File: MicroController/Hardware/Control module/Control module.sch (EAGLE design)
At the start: 78 parts, among them J1 1X2-3.5MM, J2 RJ45-TRAFO, J3 RJ45-TRAFO, J4 RJ45-TRAFO, J6 RJ11, Q1 BSS138, Q2 BSS138, Q3 BSS138, Q4 BSS138, Q5 BSS138, Q6 BSS138, Q7 BSS138, Q8 BSS138, U1 CD74HC4067SM96, U3 TLV1117-33CDCY

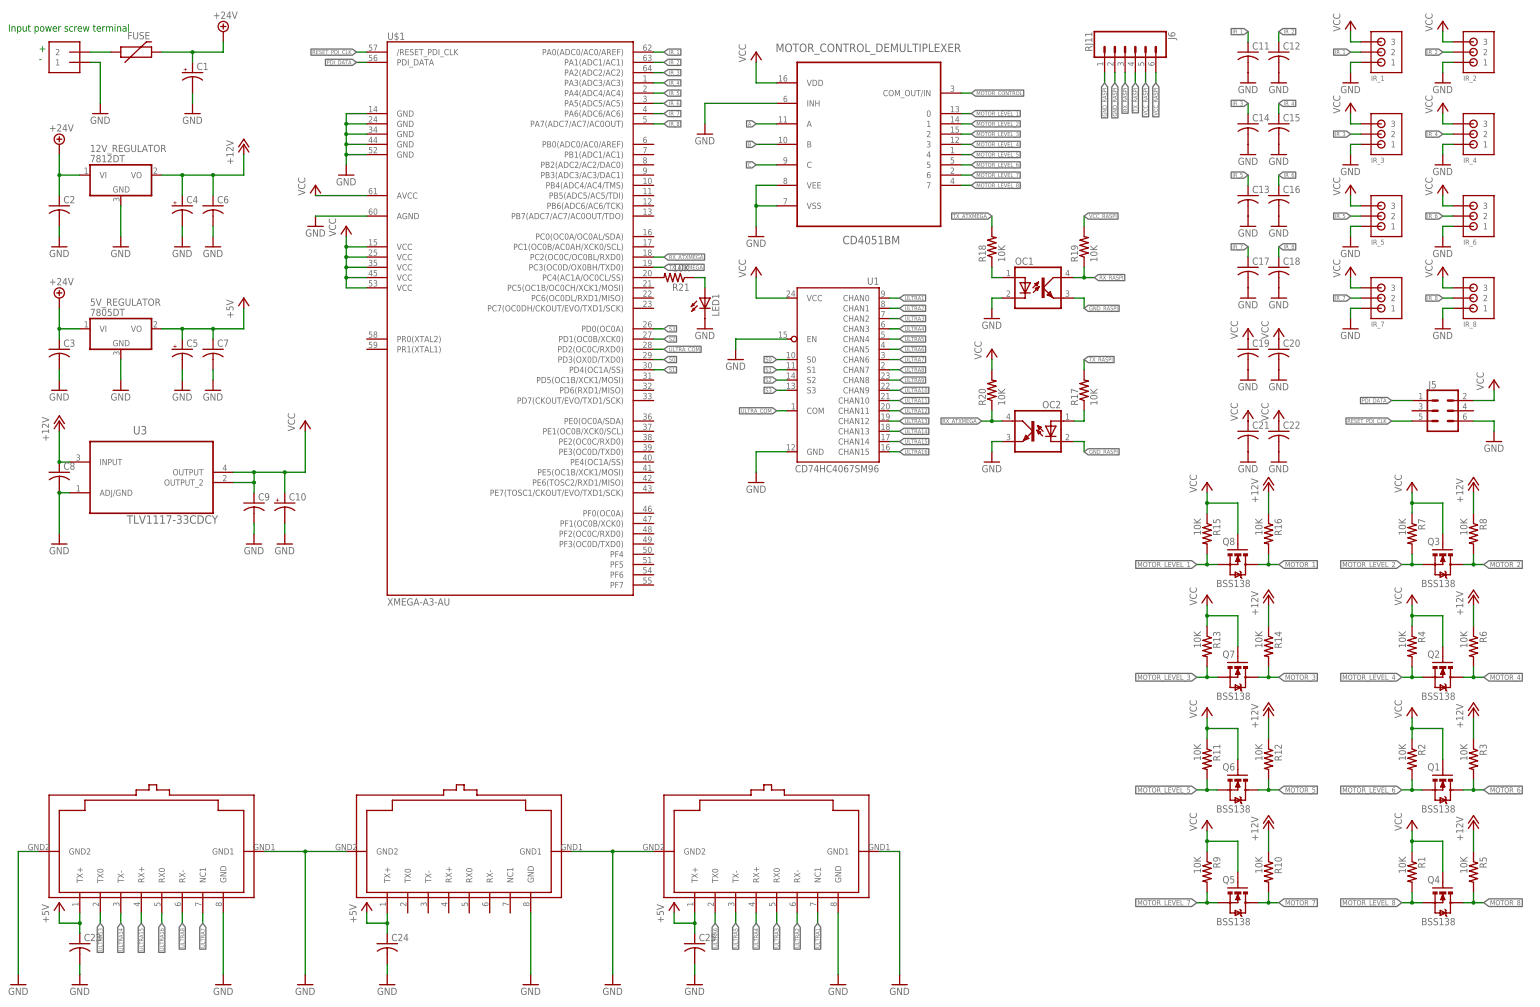
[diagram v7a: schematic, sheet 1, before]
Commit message: Changed many things in the layout.
Added more I/O and connectivity to the Raspberry Pi.
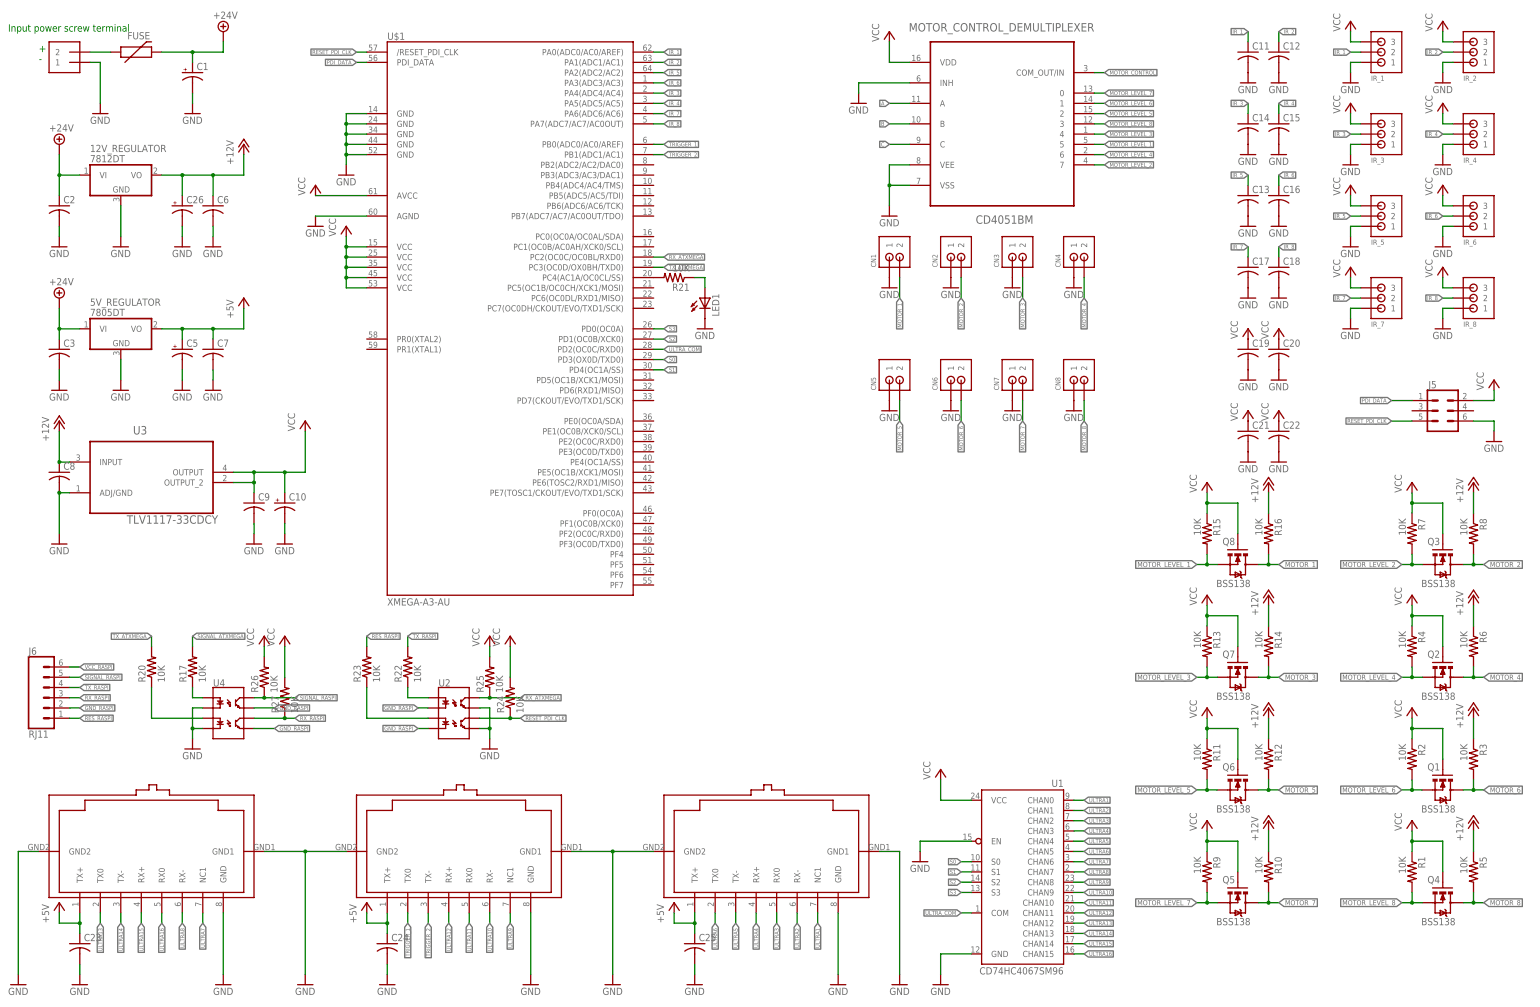
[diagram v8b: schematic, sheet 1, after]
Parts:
- removed C4: (no value), adafruit:CPOL-USE2.5-6
- removed OC1, OC2: (no value), optocoupler:PC817
- removed R18, R19: 10K, adafruit:R-US_R0805
- added C26: (no value), adafruit:CPOL-US175TMP-0810
- added CN1, CN2, CN3, CN4, CN5, CN6, CN7, CN8: JST-PH_2-PIN_HEADER, SRG:JST-PH_2-PIN_HEADER
- added R22, R23, R24, R25, R26, R27: 10K, adafruit:R-US_R0805
- added U2, U4: DUAL-OPTOISOLATOR_SOIC8, SparkFun-DiscreteSemi:DUAL-OPTOISOLATOR_SOIC8
- C1: device adafruit:CPOL-USE5-10.5 -> adafruit:CPOL-US175TMP-0810
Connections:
- removed net N$1: OC1.A, R18.1
- new net N$5: R23.1, U2.A2
- new net N$6: R22.1, U2.A1
- new net N$8: R20.1, U4.A2
- new net RES_RASPI: J6.1, R23.2
- new net SIGNAL_ATXMEGA: R17.2
- new net SIGNAL_RASPI: J6.5, R26.1, U4.CL1
- new net TRIGGER_1: J4.TX0, U$1.PB0(ADC0/AC0/AREF)
- new net TRIGGER_2: J4.TX-, U$1.PB1(ADC1/AC1)
- net +12V: now also C26.+; no longer C4.+
- net GND: now also C26.-, CN1.1, CN2.1, CN3.1, CN4.1, CN5.1, CN6.1, CN7.1, CN8.1, U2.EM1, U2.EM2, U4.C1, U4.C2; no longer C4.-, OC1.C, OC2.EMIT
- net GND_RASPI: now also U2.C1, U2.C2, U4.EM1, U4.EM2; no longer J6.1, OC1.EMIT, OC2.C
- net IR_3: now also U$1.PA4(ADC4/AC4); no longer U$1.PA2(ADC2/AC2)
- net IR_4: now also U$1.PA5(ADC5/AC5); no longer U$1.PA3(ADC3/AC3)
- net IR_5: now also U$1.PA2(ADC2/AC2); no longer U$1.PA4(ADC4/AC4)
- net IR_6: now also U$1.PA3(ADC3/AC3); no longer U$1.PA5(ADC5/AC5)
- net MOTOR_1: now also CN1.2
- net MOTOR_2: now also CN2.2
- net MOTOR_3: now also CN3.2
- net MOTOR_4: now also CN4.2
- net MOTOR_5: now also CN5.2
- net MOTOR_6: now also CN6.2
- net MOTOR_7: now also CN7.2
- net MOTOR_8: now also CN8.2
- net MOTOR_LEVEL_1: now also MOTOR_CONTROL_DEMULTIPLEXER.5; no longer MOTOR_CONTROL_DEMULTIPLEXER.0
- net MOTOR_LEVEL_2: now also MOTOR_CONTROL_DEMULTIPLEXER.7; no longer MOTOR_CONTROL_DEMULTIPLEXER.1
- net MOTOR_LEVEL_3: now also MOTOR_CONTROL_DEMULTIPLEXER.4; no longer MOTOR_CONTROL_DEMULTIPLEXER.2
- net MOTOR_LEVEL_4: now also MOTOR_CONTROL_DEMULTIPLEXER.6; no longer MOTOR_CONTROL_DEMULTIPLEXER.3
- net MOTOR_LEVEL_5: now also MOTOR_CONTROL_DEMULTIPLEXER.2; no longer MOTOR_CONTROL_DEMULTIPLEXER.4
- net MOTOR_LEVEL_6: now also MOTOR_CONTROL_DEMULTIPLEXER.1; no longer MOTOR_CONTROL_DEMULTIPLEXER.5
- net MOTOR_LEVEL_7: now also MOTOR_CONTROL_DEMULTIPLEXER.0; no longer MOTOR_CONTROL_DEMULTIPLEXER.6
- net MOTOR_LEVEL_8: now also MOTOR_CONTROL_DEMULTIPLEXER.3; no longer MOTOR_CONTROL_DEMULTIPLEXER.7
- net N$2: now also U4.A1; no longer OC2.A
- net RESET_PDI_CLK: now also R24.1, U2.CL2
- net RX_ATXMEGA: now also R25.1, U2.CL1; no longer OC2.COL, R20.1
- net RX_RASPI: now also R27.1, U4.CL2; no longer OC1.COL, R19.1
- net TX_ATXMEGA: now also R20.2; no longer R18.2
- net TX_RASPI: now also R22.2; no longer R17.2
- net ULTRA10: now also J4.RX-
- net ULTRA11: now also J4.RX0
- net ULTRA12: now also J4.RX+
- net ULTRA9: now also J4.NC1
- net VCC: now also R24.2, R25.2, R26.2, R27.2; no longer R20.2
- net VCC_RASPI: no longer J6.5, R19.2
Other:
- moved on the sheet: J6, MOTOR_CONTROL_DEMULTIPLEXER, R17, R20, U1
